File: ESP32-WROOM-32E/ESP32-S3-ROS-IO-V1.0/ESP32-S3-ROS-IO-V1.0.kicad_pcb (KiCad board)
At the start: 2 copper layers, 100 x 100 mm, 53 parts, among them J1 Conn_01x22_Socket, J16 XT60-M, J17 XT60-M, J2 Conn_01x22_Socket, J3 Conn_01x22_Socket, J4 Conn_01x22_Socket, J5 Conn_01x02_Pin, J6 Conn_01x02_Pin, SW1 SW1, SW2 SW2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

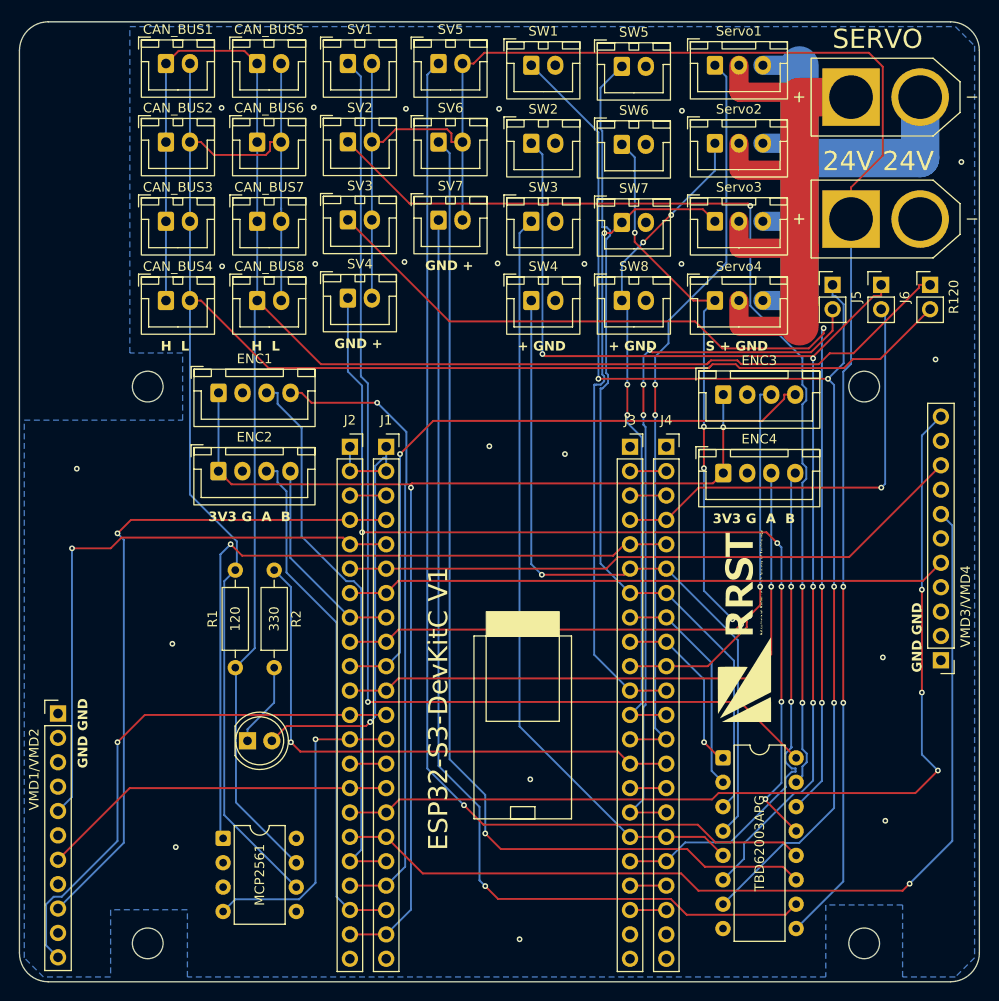
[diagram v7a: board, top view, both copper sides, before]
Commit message: 回路図変更により自動配線し直し
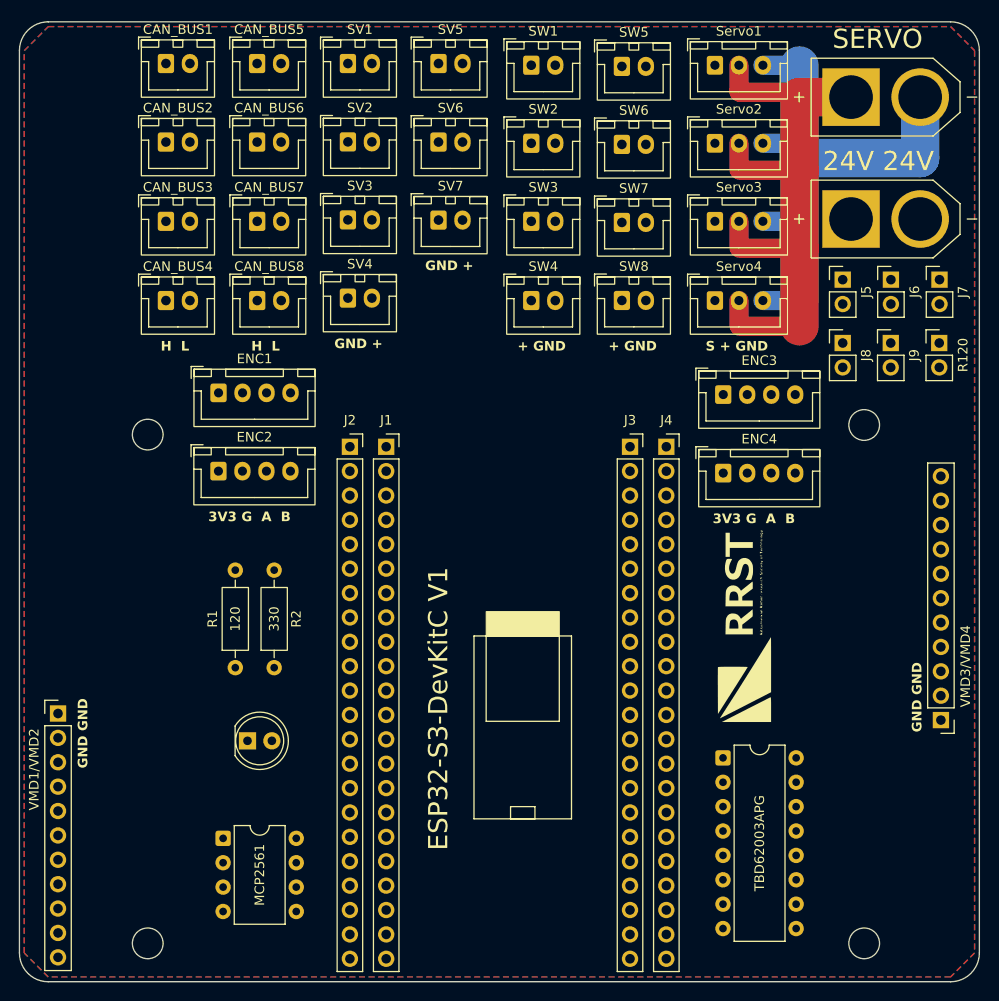
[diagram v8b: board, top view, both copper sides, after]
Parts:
- added J5: Conn_01x02_Pin, Connector_PinHeader_2.54mm:PinHeader_1x02_P2.54mm_Vertical, F.Cu at (179.8, 40.9)
- added J8: Conn_01x02_Pin, Connector_PinHeader_2.54mm:PinHeader_1x02_P2.54mm_Vertical, F.Cu at (179.8, 47.5)
- added J9: Conn_01x02_Pin, Connector_PinHeader_2.54mm:PinHeader_1x02_P2.54mm_Vertical, F.Cu at (184.8, 47.5)
- moved VMD3/VMD4 6.22 mm to (190.0, 86.7)
- moved R120 6.13 mm to (189.8, 47.5)
- moved J6 6.10 mm to (184.8, 40.9)
- moved J7 6.10 mm to (189.8, 40.9)
- moved REF4** 5.00 mm to (107.4, 57.0)
- moved REF1** 4.00 mm to (182.0, 56.0)
- renumbered J5 to J6, J6 to J7
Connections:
- J1 pad 14: GPIO46 -> NC2
- J2 pad 14: GPIO46 -> NC2
- J3 pad 15: GPIO45 -> NC5
- J3 pad 19: NC4 -> NC6
- J3 pad 2: NC2 -> NC3
- J3 pad 20: NC5 -> NC7
- J3 pad 3: NC3 -> NC4
- J4 pad 15: GPIO45 -> NC5
- J4 pad 19: NC4 -> NC6
- J4 pad 2: NC2 -> NC3
- J4 pad 20: NC5 -> NC7
- J4 pad 3: NC3 -> NC4
- J6 pad 1: TR6_Bypass_OUT -> TR4_Bypass_OUT
- J6 pad 2: GPIO48 -> GPIO42
- J7 pad 1: TR6/SW2 -> TR5_Bypass_OUT
- J7 pad 2: GPIO1 -> GPIO47
- SW1 pad 1: TR6_Bypass_OUT -> TR7_Bypass_OUT
- SW2 pad 1: TR6/SW2 -> TR6_Bypass_OUT
- SW3 pad 1: GPIO47 -> TR5_Bypass_OUT
- SW4 pad 1: GPIO42 -> TR4_Bypass_OUT
- SW5 pad 1: GPIO41 -> TR3_Bypass_OUT
- U2 pad 3: GPIO41 -> TR3_Bypass_OUT
- U2 pad 4: GPIO42 -> TR4_Bypass_OUT
- U2 pad 5: GPIO47 -> TR5_Bypass_OUT
- U2 pad 6: TR6/SW2 -> TR6_Bypass_OUT
- U2 pad 7: TR6_Bypass_OUT -> TR7_Bypass_OUT
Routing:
- net CANL: track 210.4 -> 0.00 mm
- net CANH: track 199.3 -> 0.00 mm
- net +24V: track 190.2 -> 0.00 mm, vias 2 -> 0
- net TR6_Bypass_OUT: track 131.3 -> 0.00 mm, vias 4 -> 0
- net 5VD: track 121.7 -> 0.00 mm, vias 2 -> 0
- net TR6/SW2: track 120.4 -> 0.00 mm, vias 4 -> 0
- net O5: track 116.1 -> 0.00 mm, vias 1 -> 0
- net O1: track 114.4 -> 0.00 mm, vias 1 -> 0
- net O6: track 108.4 -> 0.00 mm, vias 1 -> 0
- net O2: track 108.3 -> 0.00 mm, vias 3 -> 0
- net O3: track 107.3 -> 0.00 mm, vias 3 -> 0
- net O7: track 105.5 -> 0.00 mm, vias 1 -> 0
- net GPIO11: track 101.8 -> 0.00 mm, vias 1 -> 0
- net GPIO10: track 101.5 -> 0.00 mm, vias 3 -> 0
- net O4: track 100.9 -> 0.00 mm, vias 5 -> 0
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- added copper zone on F.Cu, net GND
